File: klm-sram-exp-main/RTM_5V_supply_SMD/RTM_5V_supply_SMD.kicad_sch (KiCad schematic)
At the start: 4 parts, among them J1 86093968114755V1LF

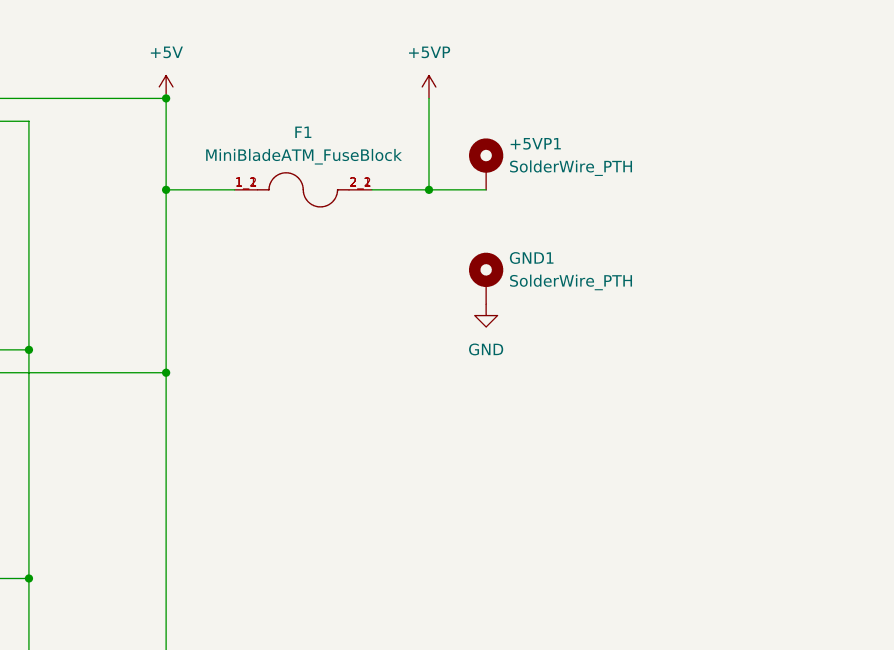
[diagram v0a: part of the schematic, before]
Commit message: Flatten nested directories, deduplicate slide PDFs
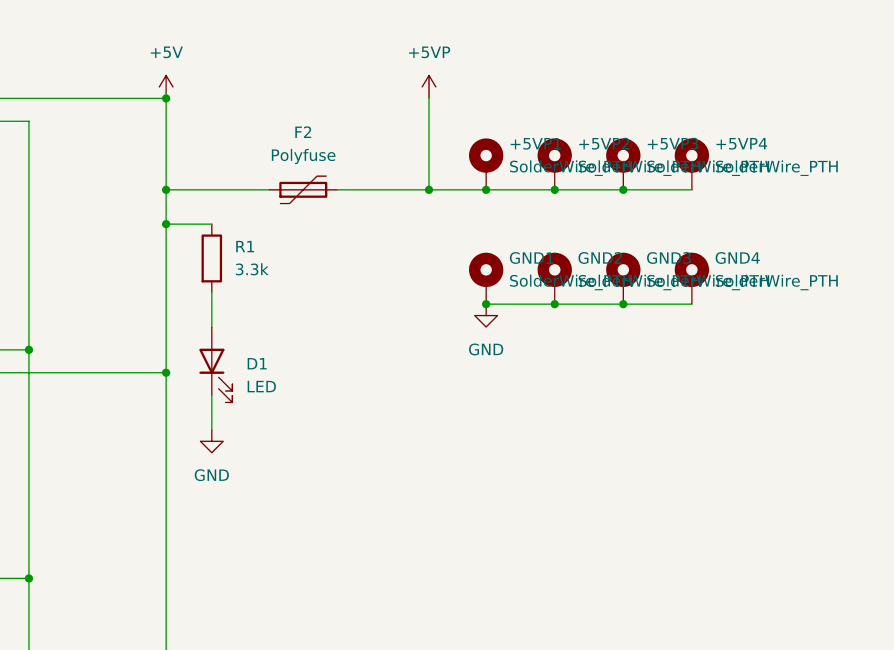
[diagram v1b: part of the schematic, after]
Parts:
- removed F1: MiniBladeATM_FuseBlock, 1_My_footprint_lib:FUSE_3544-2, symbol 1_My_kicad_symbols:3544-2
- added +5VP2, +5VP3, +5VP4, GND2, GND3, GND4: SolderWire_PTH, 1_My_footprint_lib:PTH_12AWG, symbol Mechanical:MountingHole_Pad
- added D1: LED, LED_SMD:LED_0402_1005Metric_Pad0.77x0.64mm_HandSolder, symbol Device:LED
- added F2: Polyfuse, Fuse:Fuse_Bourns_MF-RHT100, symbol Device:Polyfuse
- added R1: 3.3k, Resistor_SMD:R_0603_1608Metric_Pad0.98x0.95mm_HandSolder, symbol Device:R
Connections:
- net +5V: now also F2.1, R1.1
- net +5VP: now also +5VP2.1, +5VP3.1, +5VP4.1, F2.2
- net GND: now also D1.1 (K), GND2.1, GND3.1, GND4.1
- new net: D1.2 (A), R1.2
